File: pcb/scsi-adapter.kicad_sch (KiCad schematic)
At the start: 0 parts

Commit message: Phase 3: schematic hierarchy with empty sheets and inter-sheet nets
Root block diagram, seven A3 functional sheets, and two SCSI channel
sheet files repeated 14x (bidirectional) and 4x (receive-only).
USB_HS net-class patterns for the upstream and FT232H pairs.

Co-Authored-By: Claude Opus 5.5 <noreply@anthropic.com>
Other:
- added sheet ft232h (7-ft232h.kicad_sch)
- added sheet io (5-io.kicad_sch)
- added sheet power (1-power.kicad_sch)
- added sheet rp2350 (4-rp2350.kicad_sch)
- added sheet scsi (3-scsi.kicad_sch)
- added sheet termpwr (2-termpwr.kicad_sch)
- added sheet usb-hub (6-usb-hub.kicad_sch)
- note added: "Sheets connect by net labels on the stubs (same name = same net). Global power symbols: +5V_SYS, +3V3, VTERM (2.83 V), TERMPWR, GND. Local rails stay on their sheet: FT_3V3 (ft232h), DVDD 1.1 V (rp2350)."

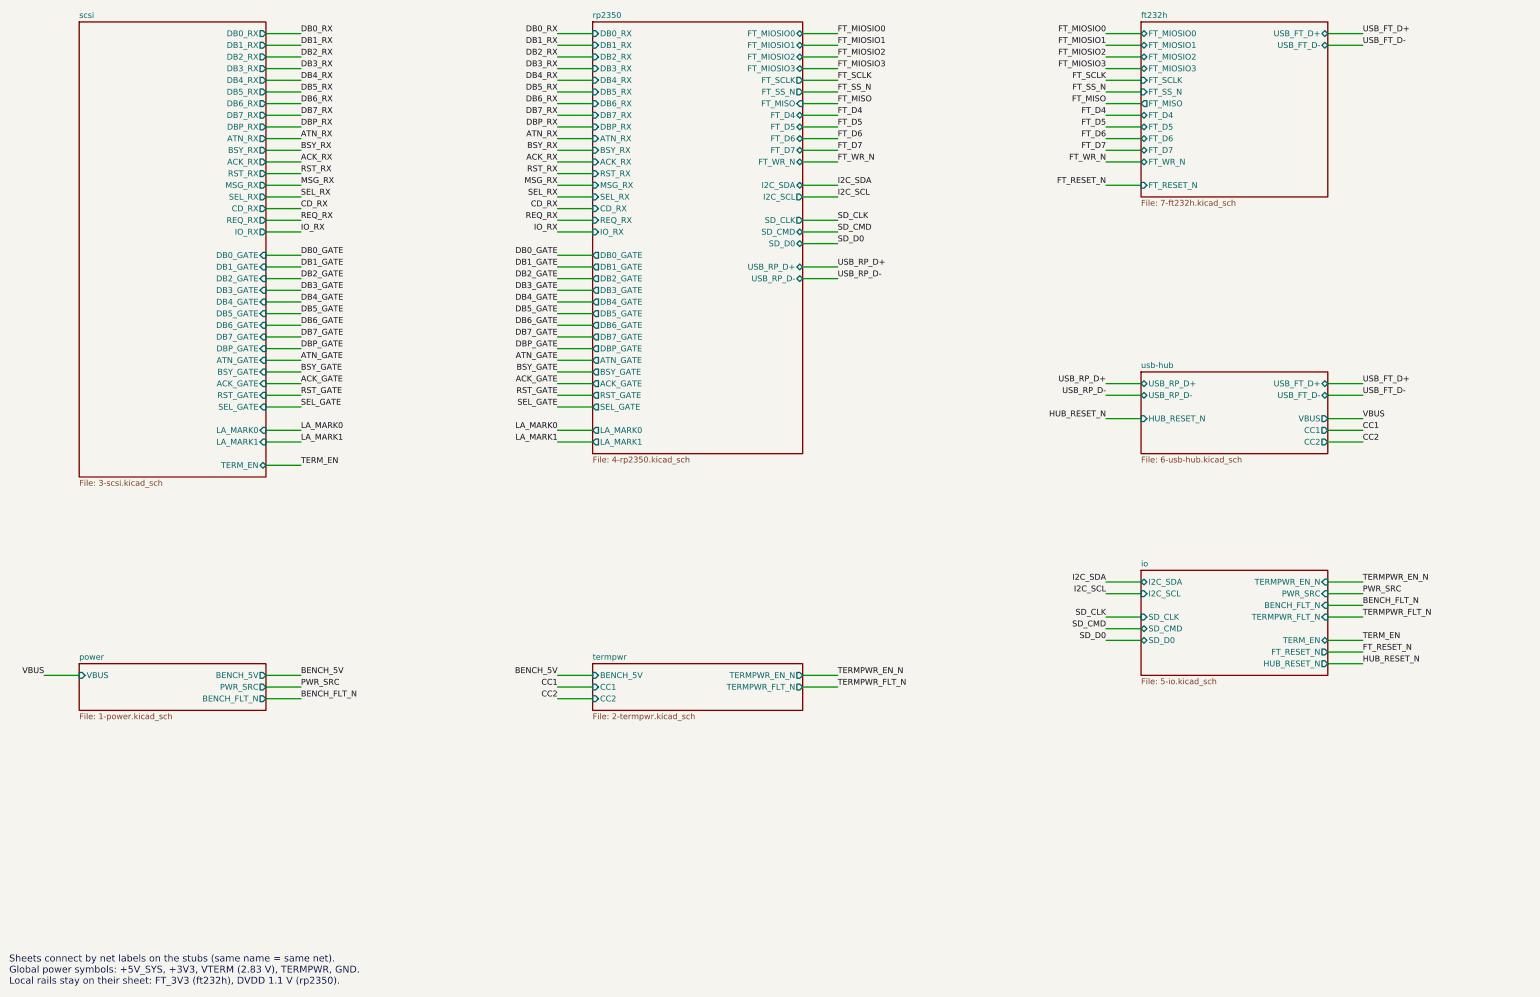
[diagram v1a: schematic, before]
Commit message: Phase 3: populate power sheet; descriptive net names
Power sheet: bench eFuse (TPS259470A) with UVLO/OVLO string and EN
clamp, TPS2116 bench-priority mux with VBUS snubber, 3.3 V and 2.83 V
TPS73701 LDOs. Notes on the string's tap voltages, eFuse setting pins
and every DNP part. Project symbol library with the TPS259470A and
TPS73701DCQ drawn from the datasheet pin tables.

Nets renamed to spelled-out names (IS_BENCH_POWERED, *_INVERTED for
active-low, FEEDBACK, VTERMINATOR, TERMINATOR_EN) across the schematic,
pinout page, parts list and power block page.

Co-Authored-By: Claude Opus 5.5 <noreply@anthropic.com>
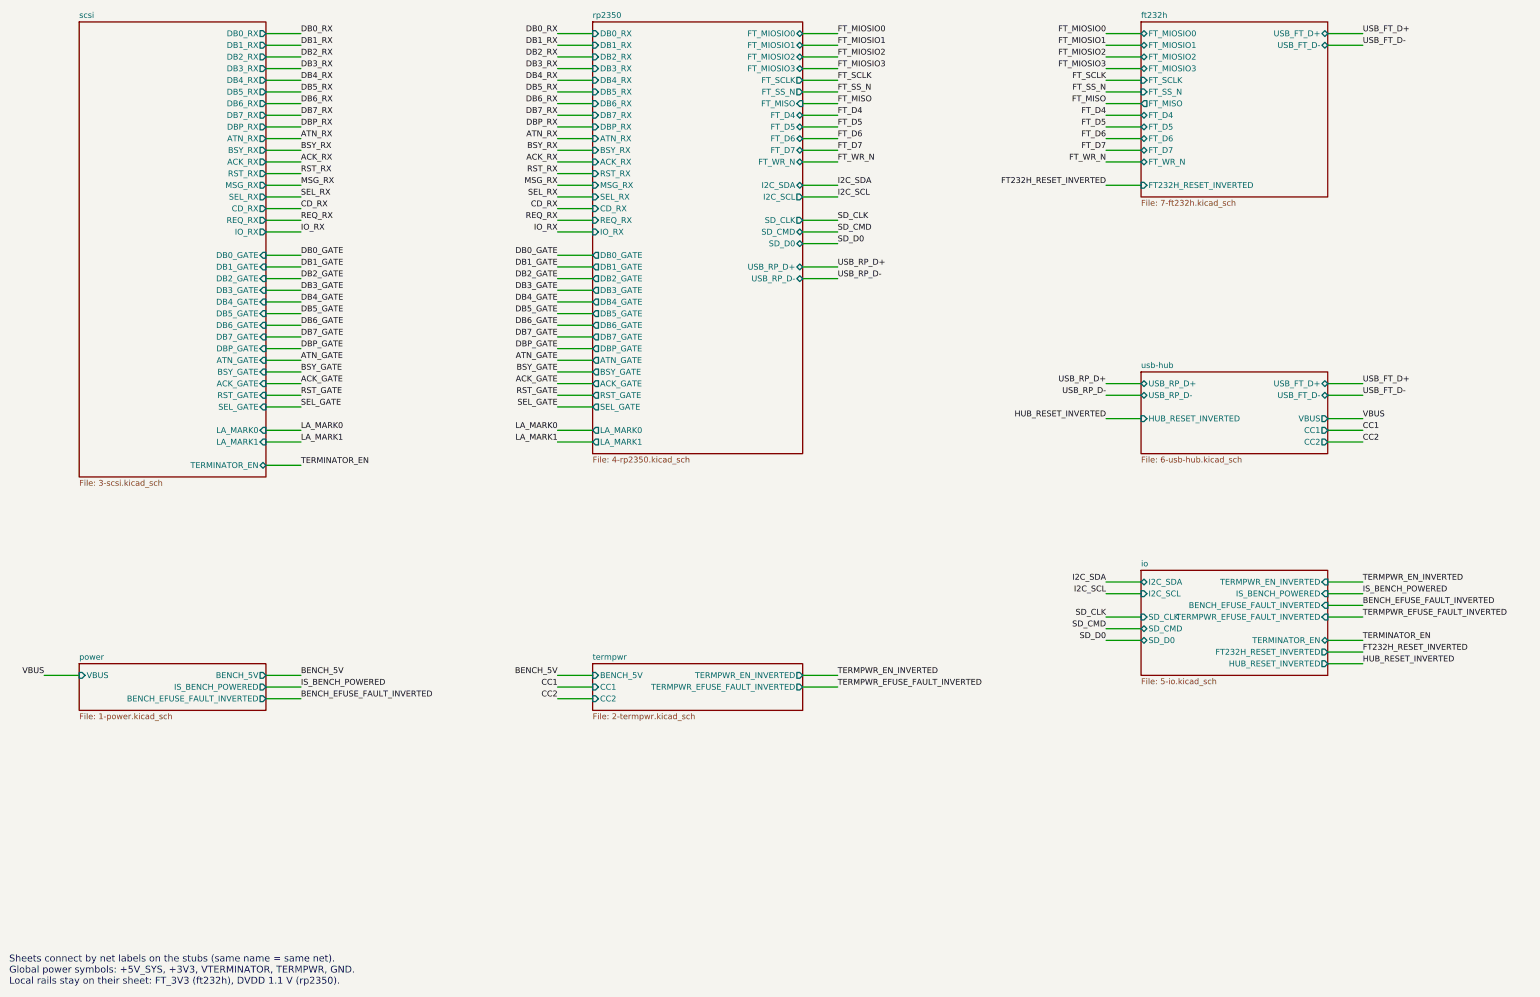
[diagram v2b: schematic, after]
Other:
- sheet ft232h ports: added FT232H_RESET_INVERTED; removed FT_RESET_N
- sheet io ports: added BENCH_EFUSE_FAULT_INVERTED, FT232H_RESET_INVERTED, HUB_RESET_INVERTED, IS_BENCH_POWERED, TERMINATOR_EN, TERMPWR_EFUSE_FAULT_INVERTED, TERMPWR_EN_INVERTED; removed BENCH_FLT_N, FT_RESET_N, HUB_RESET_N, PWR_SRC, TERMPWR_EN_N, TERMPWR_FLT_N, TERM_EN
- sheet power ports: added BENCH_EFUSE_FAULT_INVERTED, IS_BENCH_POWERED; removed BENCH_FLT_N, PWR_SRC
- sheet scsi ports: added TERMINATOR_EN; removed TERM_EN
- sheet termpwr ports: added TERMPWR_EFUSE_FAULT_INVERTED, TERMPWR_EN_INVERTED; removed TERMPWR_EN_N, TERMPWR_FLT_N
- sheet usb-hub ports: added HUB_RESET_INVERTED; removed HUB_RESET_N
- note added: "Sheets connect by net labels on the stubs (same name = same net). Global power symbols: +5V_SYS, +3V3, VTERMINATOR, TERMPWR, GND. Local rails stay on their sheet: FT_3V3 (ft232h), DVDD 1.1 V (rp2350)."
- note removed: "Sheets connect by net labels on the stubs (same name = same net). Global power symbols: +5V_SYS, +3V3, VTERM (2.83 V), TERMPWR, GND. Local rails stay on their sheet: FT_3V3 (ft232h), DVDD 1.1 V (rp2350)."
